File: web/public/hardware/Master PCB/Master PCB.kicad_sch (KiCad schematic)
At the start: 31 parts, among them J1 Rows 0-15, J10 LDR2, J11 LDR3, J12 LDR4, J13 SWD Conn, J14 LED Conn, J15 OLED1, J16 OLED2, J17 Relay Conn, J2 Cols 0-21, J3 Cols 22-31, J4 5V_IN, J5 LED1, J6 LED2, J7 LED3, J8 LED4, J9 LDR1, U6 USBLC6-4SC6, U7 USBLC6-2SC6

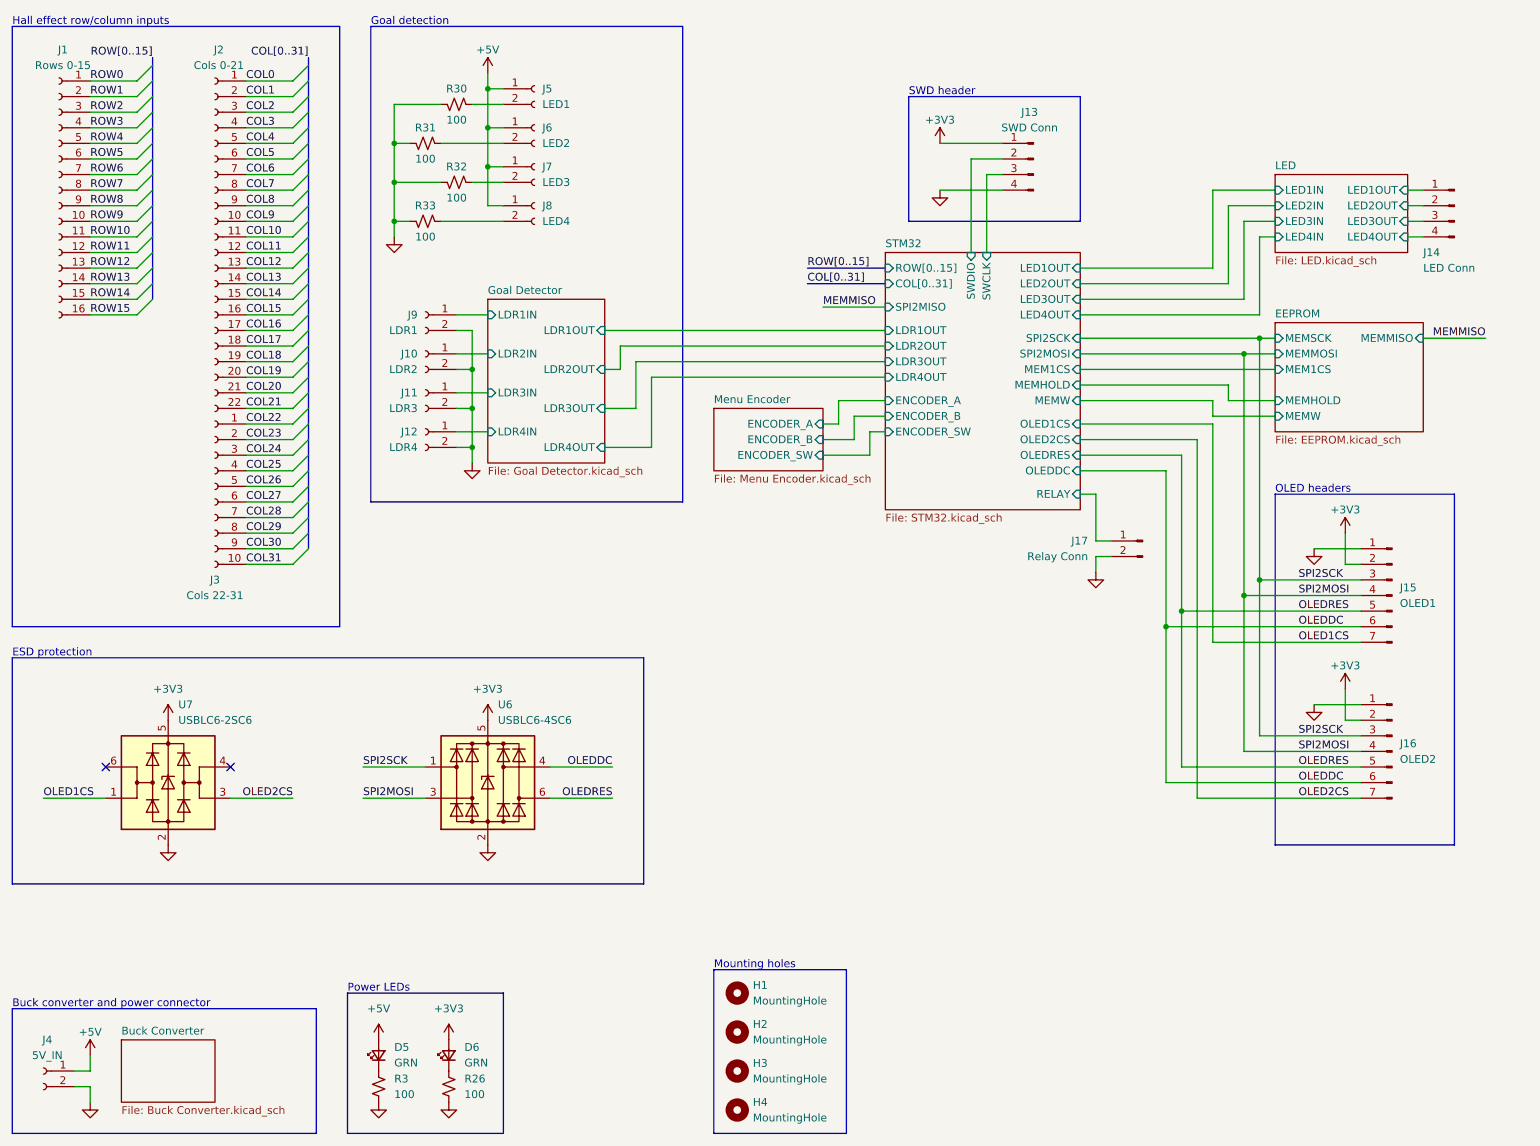
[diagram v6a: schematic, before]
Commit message: Move power indicator LEDs to buck converter schematic
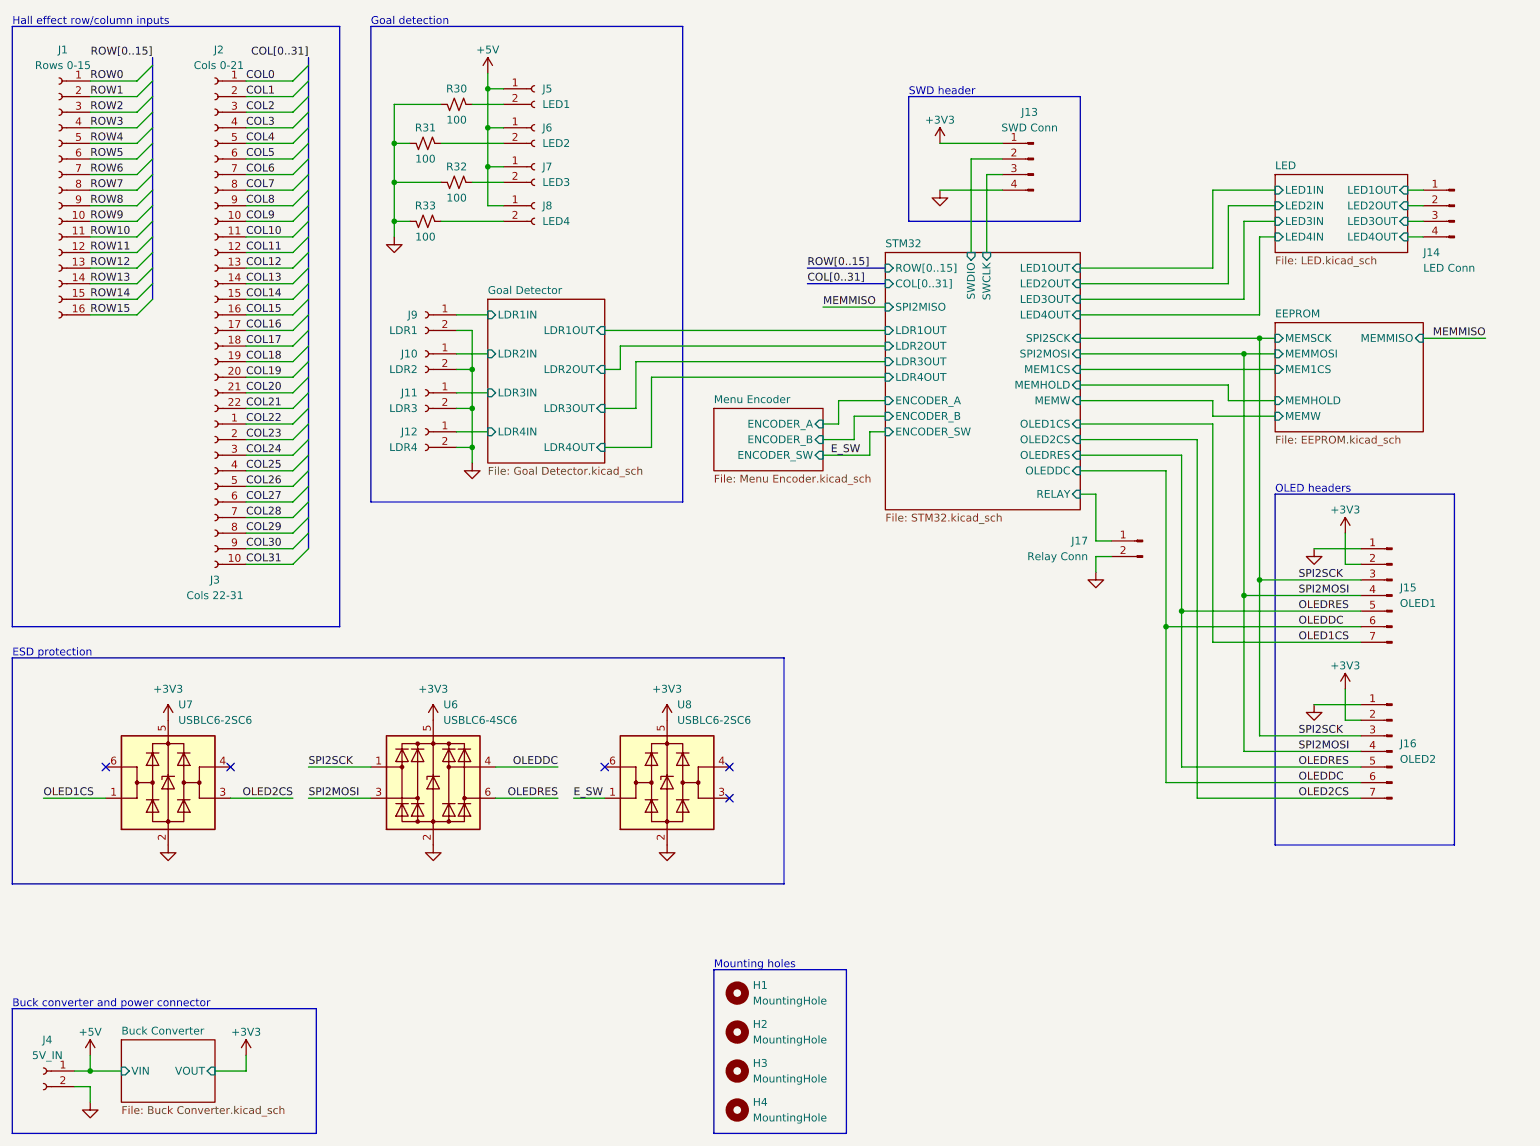
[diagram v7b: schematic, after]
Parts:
- removed D5, D6: GRN, LED_SMD:LED_0805_2012Metric_Pad1.15x1.40mm_HandSolder, symbol Device:LED_Small
- removed R26, R3: 100, Resistor_SMD:R_0805_2012Metric_Pad1.20x1.40mm_HandSolder, symbol Device:R_Small_US
- added U8: USBLC6-2SC6, Package_TO_SOT_SMD:SOT-23-6, symbol Power_Protection:USBLC6-2SC6
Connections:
- net +3V3: now also U8.5 (VBUS)
- net GND: now also U8.2 (GND)
- new net E_SW: U8.1 (I/O1)
- no-connect marks 2 -> 5
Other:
- sheet Buck Converter ports: added VIN, VOUT; removed none
- note removed: "Power LEDs"
- moved on the sheet: U6

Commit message: Schematic cleanup
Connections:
- net E_SW renamed ENCODER_SW
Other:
- moved on the sheet: U8
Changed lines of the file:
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@@
   (junction (at 205.74 115.57) (diameter 0) (color 0 0 0 0)
   )
-  (no_connect (at 114.3 138.43))
+  (no_connect (at 121.92 138.43))
   (no_connect (at 53.34 138.43))
-  (no_connect (at 134.62 143.51))
+  (no_connect (at 142.24 143.51))
   (no_connect (at 33.02 138.43))
-  (no_connect (at 134.62 138.43))
+  (no_connect (at 142.24 138.43))
   (bus_entry (at 66.04 77.47) (size -2.54 2.54)
     (stroke (width 0) (type default))
@@
     (stroke (width 0) (type default))
   )
-  (wire (pts (xy 109.22 143.51) (xy 114.3 143.51))
-    (stroke (width 0) (type default))
-  )
   (wire (pts (xy 223.52 78.74) (xy 215.9 78.74))
     (stroke (width 0) (type default))
@@
     (stroke (width 0) (type default))
   )
+  (wire (pts (xy 109.22 143.51) (xy 121.92 143.51))
+    (stroke (width 0) (type default))
+  )
   (wire (pts (xy 95.25 34.29) (xy 95.25 40.64))
     (stroke (width 0) (type default))
@@
     (fill (type none))
   )
-  (rectangle (start 17.78 120.65) (end 143.51 157.48)
+  (rectangle (start 17.78 120.65) (end 151.13 157.48)
     (stroke (width 0) (type default))
     (fill (type none))
@@
     (effects (font (size 1.27 1.27)) (justify left bottom))
   )
-  (label "E_SW" (at 151.13 87.63 0) (fields_autoplaced)
-    (effects (font (size 1.27 1.27)) (justify left bottom))
+  (label "ENCODER_SW" (at 157.48 87.63 180) (fields_autoplaced)
+    (effects (font (size 0.75 0.75)) (justify right bottom))
   )
   (label "OLEDDC" (at 227.33 115.57 0) (fields_autoplaced)
@@
     (effects (font (size 1.27 1.27)) (justify left bottom))
   )
-  (label "E_SW" (at 109.22 143.51 0) (fields_autoplaced)
+  (label "ENCODER_SW" (at 109.22 143.51 0) (fields_autoplaced)
     (effects (font (size 1.27 1.27)) (justify left bottom))
   )
@@
     )
   )
-  (symbol (lib_id "power:+3V3") (at 124.46 130.81 0) (unit 1)
+  (symbol (lib_id "power:+3V3") (at 132.08 130.81 0) (unit 1)
     (in_bom yes) (on_board yes) (dnp no) (fields_autoplaced)
-    (property "Reference" "#PWR084" (at 124.46 134.62 0)
-      (effects (font (size 1.27 1.27)) hide)
-    )
-    (property "Value" "+3V3" (at 124.46 125.73 0)
-      (effects (font (size 1.27 1.27)))
-    )
-    (property "Footprint" "" (at 124.46 130.81 0)
-      (effects (font (size 1.27 1.27)) hide)
-    )
-    (property "Datasheet" "" (at 124.46 130.81 0)
+    (property "Reference" "#PWR084" (at 132.08 134.62 0)
+      (effects (font (size 1.27 1.27)) hide)
+    )
+    (property "Value" "+3V3" (at 132.08 125.73 0)
+      (effects (font (size 1.27 1.27)))
+    )
+    (property "Footprint" "" (at 132.08 130.81 0)
+      (effects (font (size 1.27 1.27)) hide)
+    )
+    (property "Datasheet" "" (at 132.08 130.81 0)
       (effects (font (size 1.27 1.27)) hide)
     )
@@
     )
   )
-  (symbol (lib_id "Power_Protection:USBLC6-2SC6") (at 124.46 140.97 0) (unit 1)
+  (symbol (lib_id "Power_Protection:USBLC6-2SC6") (at 132.08 140.97 0) (unit 1)
     (in_bom yes) (on_board yes) (dnp no) (fields_autoplaced)
-    (property "Reference" "U8" (at 126.1111 128.27 0)
-      (effects (font (size 1.27 1.27)) (justify left))
-    )
-    (property "Value" "USBLC6-2SC6" (at 126.1111 130.81 0)
-      (effects (font (size 1.27 1.27)) (justify left))
-    )
-    (property "Footprint" "Package_TO_SOT_SMD:SOT-23-6" (at 124.46 153.67 0)
-      (effects (font (size 1.27 1.27)) hide)
-    )
-    (property "Datasheet" "https://www.st.com/resource/en/datasheet/usblc6-2.pdf" (at 129.54 132.08 0)
+    (property "Reference" "U8" (at 133.7311 128.27 0)
+      (effects (font (size 1.27 1.27)) (justify left))
+    )
+    (property "Value" "USBLC6-2SC6" (at 133.7311 130.81 0)
+      (effects (font (size 1.27 1.27)) (justify left))
+    )
+    (property "Footprint" "Package_TO_SOT_SMD:SOT-23-6" (at 132.08 153.67 0)
+      (effects (font (size 1.27 1.27)) hide)
+    )
+    (property "Datasheet" "https://www.st.com/resource/en/datasheet/usblc6-2.pdf" (at 137.16 132.08 0)
       (effects (font (size 1.27 1.27)) hide)
     )
@@
     )
   )
-  (symbol (lib_id "power:GND") (at 124.46 151.13 0) (unit 1)
+  (symbol (lib_id "power:GND") (at 132.08 151.13 0) (unit 1)
     (in_bom yes) (on_board yes) (dnp no) (fields_autoplaced)
-    (property "Reference" "#PWR085" (at 124.46 157.48 0)
-      (effects (font (size 1.27 1.27)) hide)
-    )
-    (property "Value" "GND" (at 124.46 156.21 0)
-      (effects (font (size 1.27 1.27)) hide)
-    )
-    (property "Footprint" "" (at 124.46 151.13 0)
-      (effects (font (size 1.27 1.27)) hide)
-    )
-    (property "Datasheet" "" (at 124.46 151.13 0)
-      (effects (font (size 1.27 1.27)) hide)
-    )
+    (property "Reference" "#PWR085" (at 132.08 157.48 0)
+      (effects (font (size 1.27 1.27)) hide)
+    )
+    (property "Value" "GND" (at 132.08 156.21 0)
+      (effects (font (size 1.27 1.27)) hide)
+    )
+    (property "Footprint" "" (at 132.08 151.13 0)
+      (effects (font (size 1.27 1.27)) hide)
+    )
+    (property "Datasheet" "" (at 132.08 151.13 0)
+      (effects (font (size 1.27 1.27)) hide)
+    )
